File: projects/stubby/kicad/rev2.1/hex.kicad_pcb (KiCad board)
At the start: 2 copper layers, 49.5 x 49.5 mm, 72 parts, among them IC1 ATMEGA1284-A, P1 BATT (4.8V-6V), P10 CONN_4, P11 CONN_4, P2 PROG, P3 CONN_10, P4 CONN_6, P5 CONN_13, P6 CONN_6, P7 CONN_1, P8 CONN_6, P9 CONN_2, SW1 DPDT, SW2 SW_PUSH, U1 HMC5883L, X1 CRYSTAL

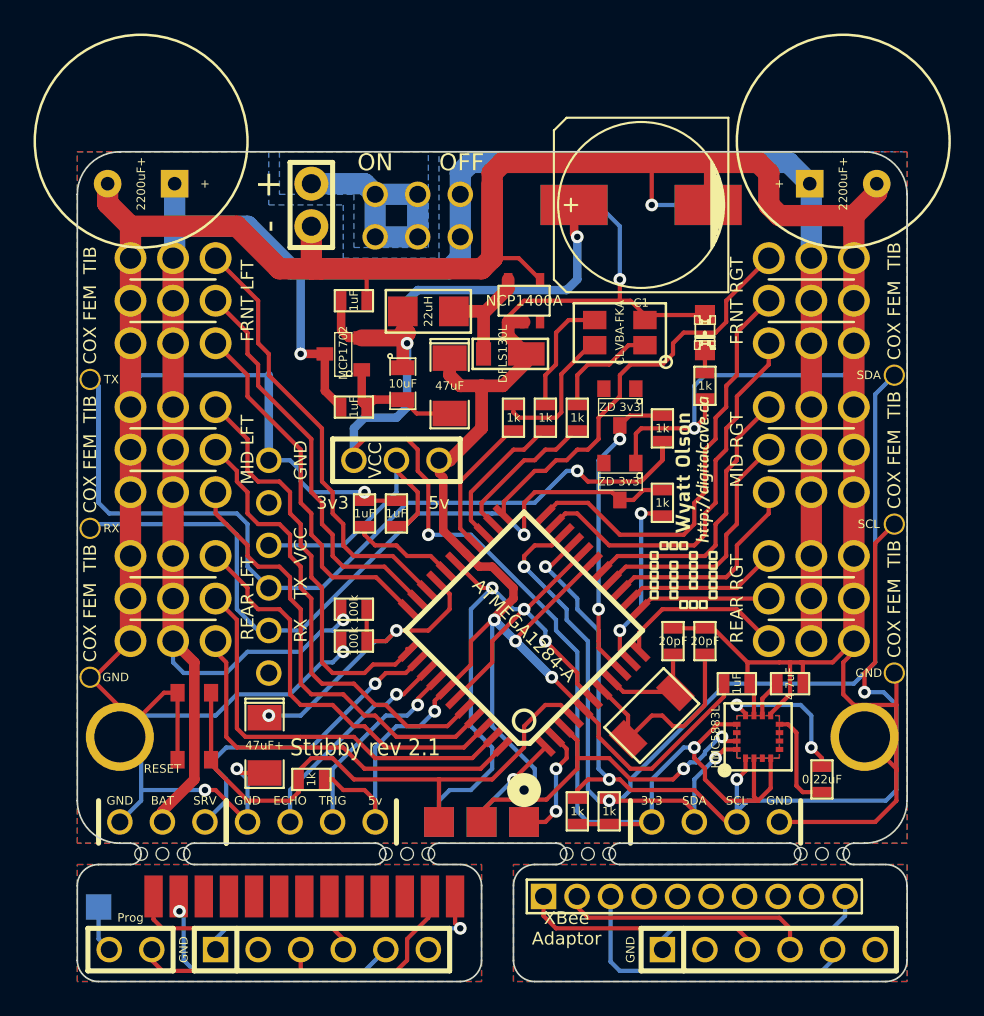
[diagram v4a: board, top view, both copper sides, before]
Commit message: Rev 2.1 board changes
-Removed the resistor and zener from the AVR_RX / MODULE_TX trace.  Now
the module talks directly to the AVR without any interference (there
were problems with my rev 2.0 board on this item...)
-Compacted the SMD components a bit more
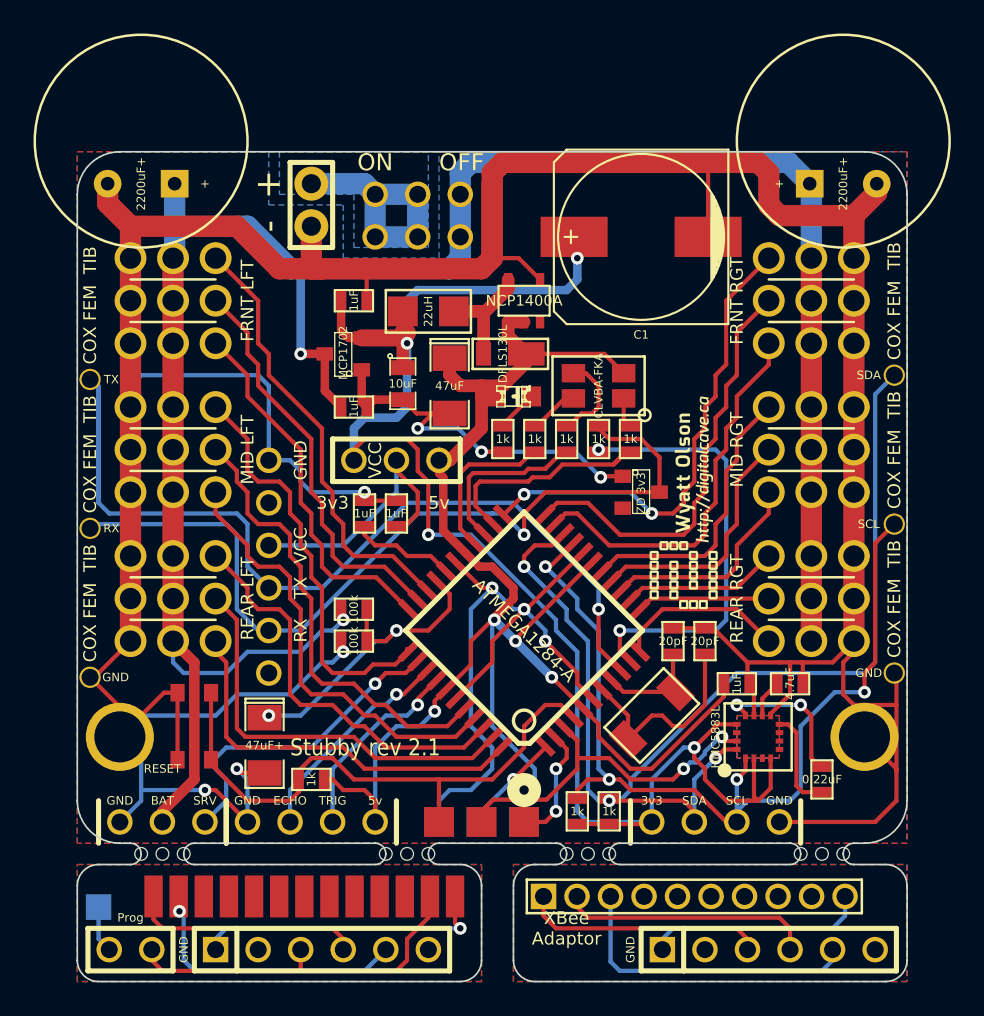
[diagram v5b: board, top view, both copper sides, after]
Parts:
- removed C8: 2200uF+, c_elec_10x10
- removed R9: 1k, SM0603_VALUE
- removed ZD1: ZD 3v3, SOT23
- moved R1 12.5 mm to (61.0, 31.8)
- moved D2 12.0 mm to (61.6, 29.2), turned to 0 degrees
- moved R8 5.39 mm to (66.7, 31.8)
- moved D3 3.42 mm to (66.7, 28.6)
- moved R7 3.42 mm to (68.6, 31.8)
- moved C1 1.90 mm to (69.2, 19.7)
- moved R5 1.80 mm to (62.9, 31.8)
- moved R6 1.80 mm to (64.8, 31.8)
- moved ZD2 1.42 mm to (69.2, 34.9), turned to 270 degrees
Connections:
- 1PIN pad 1: /MODULE_TX -> /AVR_RX
- P6 pad 4: /MODULE_TX -> /AVR_RX
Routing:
- net /MODULE_TX: track 58.4 -> 0.00 mm, vias 1 -> 0
- net /AVR_RX: track 18.4 -> 58.3 mm, vias 2 -> 1
- net /AVR_TX: track 10.9 -> 26.2 mm
- net +5V: track 110.6 -> 96.8 mm, vias 5 -> 4
- net GND: track 320.3 -> 311.3 mm, vias 9 -> 10
- net /MODULE_RX: track 45.5 -> 51.1 mm
- net /LED_GR_R: track 8.56 -> 3.00 mm
- net /LED_RD: track 9.14 -> 14.0 mm
- net /LED_RD_R: track 6.56 -> 1.83 mm
- net /I2C_SCL: track 60.6 -> 56.1 mm
- net /PWM03: track 25.3 -> 28.8 mm, vias 0 -> 2
- net +3.3V: track 98.9 -> 97.0 mm
- net /LED_BL_R: track 7.20 -> 5.46 mm
- net /LED_BL: track 8.83 -> 10.3 mm
- net N-000003: track 1.36 -> 2.48 mm
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
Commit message: Moving the 3v3 rail to another regulator, after the 5v one.  In rev 2.0, the 5v output is very smooth while the 3v3 output is noisy; this causes the magnetometer to hang when the battery starts to get low, which in turn hangs the program and causes a restart.  This change should fix that.
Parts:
- added C17: 1uF, SM0603_VALUE, F.Cu at (65.4, 24.8)
- added C18: 470uF, C1V5, F.Cu at (71.1, 19.7)
- added C8: 1uF, SM0603_VALUE, F.Cu at (71.8, 24.8)
- added VR3: MCP1702, SOT23, F.Cu at (68.6, 24.1)
- C1: footprint c_elec_10x10 -> C1V7
- moved C1 5.12 mm to (64.8, 17.1), turned to 0 degrees
- turned R1 to 90 degrees
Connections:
- C1 pad 1: +3.3V -> N-0000084
- C2 pad 1: +3.3V -> N-0000084
- C6 pad 1: +3.3V -> N-0000084
- D2 pad 2: N-000003 (its old number) -> N-0000019
- L1 pad 1: +3.3V -> N-0000084
- R1 pad 1: N-000003 (its old number) -> GND
- R1 pad 2: GND -> N-0000019
- VR1 pad 3: +3.3V -> N-0000084
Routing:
- net N-0000084: track 0.00 -> 26.3 mm, vias 0 -> 1
- net +5V: track 96.8 -> 109.4 mm
- net GND: track 311.3 -> 318.7 mm
- net +3.3V: track 97.0 -> 90.6 mm, vias 4 -> 3
- net N-000003 (its old number): track 2.48 -> 0.00 mm
- net N-0000019: track 0.00 -> 2.48 mm

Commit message: Reannotated schematic
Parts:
- renumbered C6 to C1, C7 to C10, C18 to C11, C9 to C12, C8 to C13, C17 to C14, C10 to C15, C14 to C16, C4 to C17, C5 to C18, C1 to C2, C2 to C3, C3 to C4, C13 to C5, C15 to C6, C11 to C7, C12 to C8, C16 to C9, P4 to P1, P11 to P10, P6 to P11, P8 to P2, P5 to P4, P10 to P5, P9 to P6, P1 to P8, P2 to P9, R10 to R1, R7 to R10, R11 to R2, R4 to R3, R1 to R4, R2 to R5, R3 to R6, R8 to R7, R5 to R8, R6 to R9, S7 to S1, S1 to S2, S2 to S3, S3 to S4, S4 to S5, S5 to S6, S6 to S7, SW2 to SW1, SW1 to SW2, ZD2 to ZD1

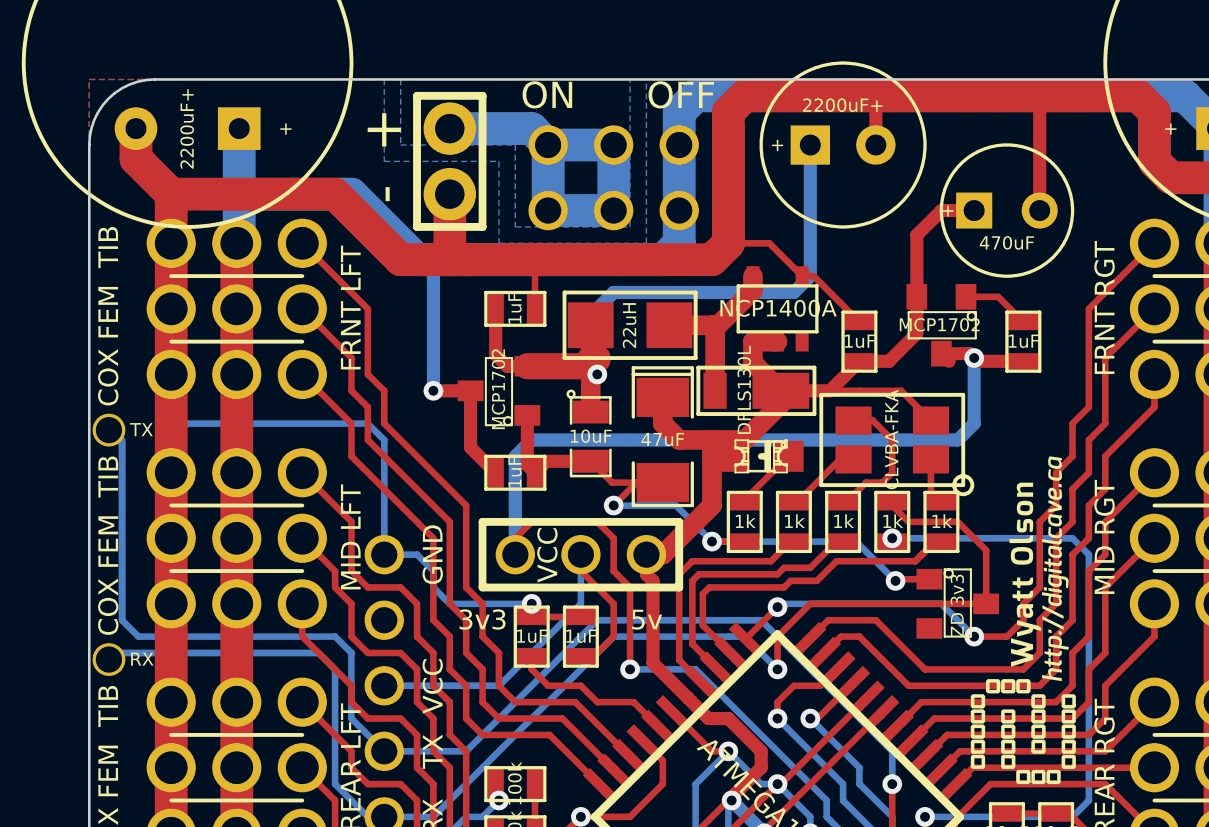
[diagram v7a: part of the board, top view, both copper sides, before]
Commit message: -Fix incorrect pinout in MCP1702 -Move some SMD components around for better fit
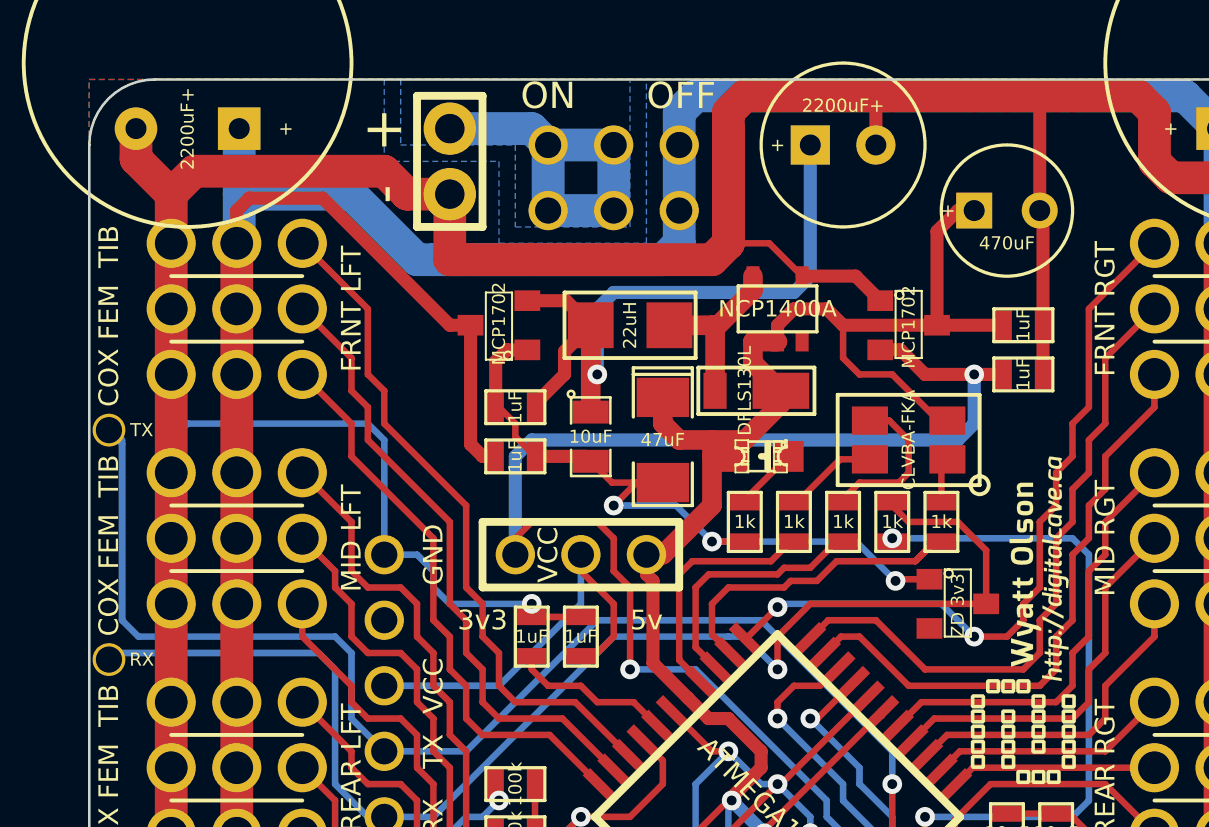
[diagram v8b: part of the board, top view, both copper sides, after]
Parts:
- moved C14 6.38 mm to (71.8, 24.1), turned to 0 degrees
- moved C3 3.81 mm to (52.1, 27.3), turned to 180 degrees
- moved VR1 2.54 mm to (51.4, 24.1)
- moved C13 1.27 mm to (71.8, 26.0), turned to 0 degrees
- moved VR3 1.27 mm to (67.3, 24.1), turned to 270 degrees
- moved D3 0.64 mm to (67.3, 28.6)
- moved C4 0.63 mm to (52.1, 29.2)
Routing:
- net +BATT: track 135.7 -> 143.9 mm, vias 2 -> 1
- net GND: track 318.7 -> 323.3 mm
- net +5V: track 109.4 -> 112.2 mm
- net /LED_RD: track 14.0 -> 13.2 mm
- net /LED_BL_R: track 5.46 -> 6.17 mm
- net /LED_GR_R: track 3.00 -> 3.63 mm
- net N-0000084: track 26.3 -> 26.9 mm
